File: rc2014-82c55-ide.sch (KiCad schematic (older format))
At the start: 22 parts, among them J1 CONN_01X02, J2 IDE connector, J3 IDE connector, J5 CONN_01X03, P1 RC2014 BUS, SW1 SW_DIP_x06, U1 82C55A_PLCC, U2 74HCT688, U3 74HCT04

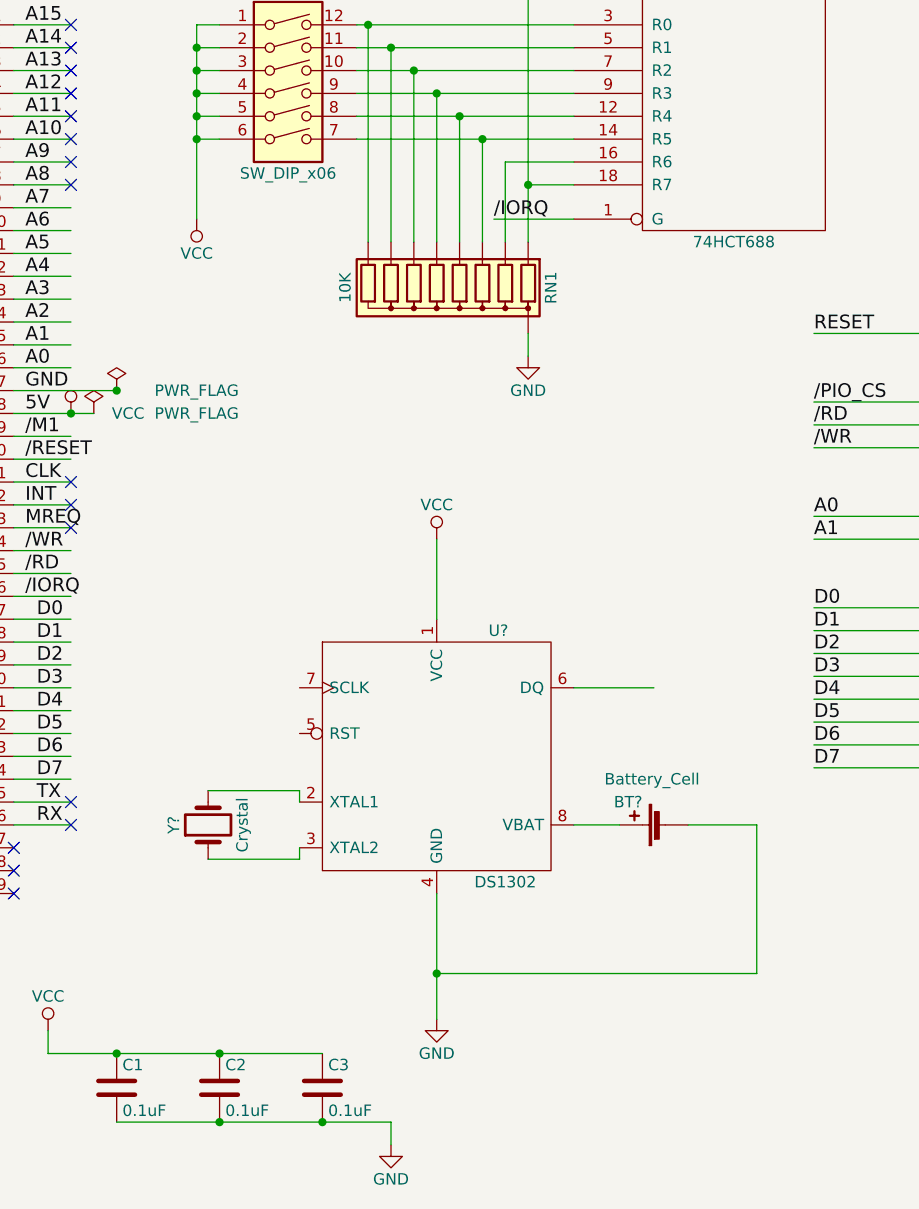
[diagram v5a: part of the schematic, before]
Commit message: remove clock
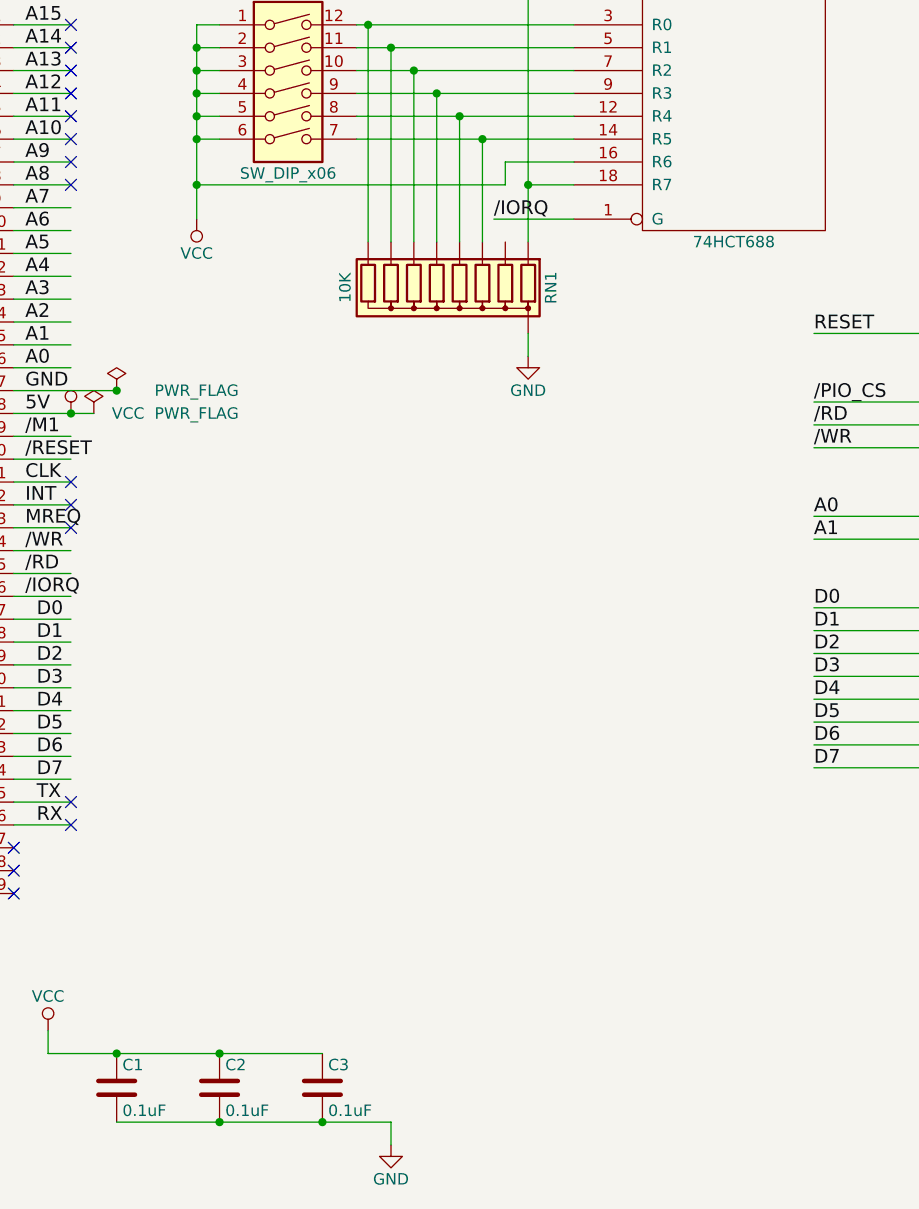
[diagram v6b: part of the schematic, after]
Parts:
- removed BT?: Battery_Cell, symbol Battery_Cell
- removed U?: DS1302, symbol DS1302
- removed Y?: Crystal, symbol Crystal
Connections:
- wire segments 243 -> 233
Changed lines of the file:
@@
 	3350 1650 3350 2750
-Wire Wire Line
-	3250 2750 3250 2400
 Wire Wire Line
 	3150 2750 3150 2300
@@
 Text Label 8650 4900 0    60   ~ 0
 DIOR
-$Comp
-L DS1302 U?
-U 1 1 59C5373F
-P 2950 5000
-F 0 "U?" H 3220 5550 50  0000 C CNN
-F 1 "DS1302" H 3250 4450 50  0000 C CNN
-F 2 "" H 2950 5000 50  0000 C CNN
-F 3 "" H 2950 5000 50  0000 C CNN
-	1    2950 5000
-	1    0    0    -1
-$EndComp
-$Comp
-L Crystal Y?
-U 1 1 59C537A8
-P 1950 5300
-F 0 "Y?" H 1950 5450 50  0000 C CNN
-F 1 "Crystal" H 1950 5150 50  0000 C CNN
-F 2 "" H 1950 5300 50  0000 C CNN
-F 3 "" H 1950 5300 50  0000 C CNN
-	1    1950 5300
-	0    -1   -1   0
-$EndComp
-$Comp
-L Battery_Cell BT?
-U 1 1 59C53806
-P 3950 5300
-F 0 "BT?" V 4050 5400 50  0000 L CNN
-F 1 "Battery_Cell" V 4150 5150 50  0000 L CNN
-F 2 "" V 3950 5360 50  0000 C CNN
-F 3 "" V 3950 5360 50  0000 C CNN
-	1    3950 5300
-	0    -1   -1   0
-$EndComp
-Wire Wire Line
-	2950 4050 2950 4400
-Wire Wire Line
-	2950 5600 2950 6150
-Wire Wire Line
-	3550 4700 3900 4700
-Wire Wire Line
-	3750 5300 3550 5300
-Wire Wire Line
-	4050 5300 4350 5300
-Wire Wire Line
-	4350 5300 4350 5950
-Wire Wire Line
-	4350 5950 2950 5950
-Connection ~ 2950 5950
-$Comp
-L GND #PWR?
-U 1 1 59C54569
-P 2950 6150
-F 0 "#PWR?" H 2950 5900 50  0001 C CNN
-F 1 "GND" H 2950 6000 50  0000 C CNN
-F 2 "" H 2950 6150 50  0000 C CNN
-F 3 "" H 2950 6150 50  0000 C CNN
-	1    2950 6150
-	1    0    0    -1
-$EndComp
-$Comp
-L VCC #PWR?
-U 1 1 59C545CE
-P 2950 4050
-F 0 "#PWR?" H 2950 3900 50  0001 C CNN
-F 1 "VCC" H 2950 4200 50  0000 C CNN
-F 2 "" H 2950 4050 50  0000 C CNN
-F 3 "" H 2950 4050 50  0000 C CNN
-	1    2950 4050
-	1    0    0    -1
-$EndComp
-Wire Wire Line
-	1950 5450 2350 5450
-Wire Wire Line
-	2350 5450 2350 5400
-Wire Wire Line
-	2350 5200 2350 5150
-Wire Wire Line
-	2350 5150 1950 5150
+Wire Wire Line
+	3250 2400 3250 2500
+Wire Wire Line
+	3250 2500 1900 2500
+Connection ~ 1900 2500
 $EndSCHEMATC

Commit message: WIP
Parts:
- JP1, JP2, JP3, JP4: footprint (none) -> Pin_Headers:Pin_Header_Straight_1x03_Pitch2.54mm
- RN1: footprint Resistors_THT:R_Array_SIP9 -> Resistors_THT:R_Array_SIP8; symbol R_Network08 -> R_Network07
- SW1: symbol SW_DIP_x06 -> SW_DIP_x06-RESCUE-rc2014-82c55-ide
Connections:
- wire segments 233 -> 234

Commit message: R1 as submitted to allpcb
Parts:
- added R2, R3, R4: 10K, Resistors_THT:R_Axial_DIN0207_L6.3mm_D2.5mm_P7.62mm_Horizontal, symbol R
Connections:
- net labels added: CSEL, DMACK, DMARQ
- wire segments 234 -> 242
- no-connect marks 32 -> 26
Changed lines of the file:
@@
 Text Label 8950 3200 0    60   ~ 0
 DA2
-NoConn ~ 7650 2500
 NoConn ~ 7650 2800
-NoConn ~ 7650 2900
-NoConn ~ 9150 2800
 NoConn ~ 9150 3000
 NoConn ~ 9150 3100
@@
 Text Label 10650 3200 0    60   ~ 0
 DA2
-NoConn ~ 9350 2500
 NoConn ~ 9350 2800
-NoConn ~ 9350 2900
-NoConn ~ 10850 2800
 NoConn ~ 10850 3000
 NoConn ~ 10850 3100
@@
 Text Label 7950 5200 0    60   ~ 0
 PC6
+Text Label 7650 2500 0    60   ~ 0
+DMARQ
+Text Label 9350 2500 0    60   ~ 0
+DMARQ
+Text Label 7650 2900 0    60   ~ 0
+DMACK
+Text Label 9350 2900 0    60   ~ 0
+DMACK
+Text Label 8750 2800 0    60   ~ 0
+CSEL
+Text Label 10450 2800 0    60   ~ 0
+CSEL
+Text Label 8700 3650 0    60   ~ 0
+CSEL
+Wire Wire Line
+	9100 3650 8600 3650
+Wire Wire Line
+	8600 3650 8600 3800
+Connection ~ 8600 3800
+Wire Wire Line
+	7500 950  7850 950
+$Comp
+L R R3
+U 1 1 59C99AC5
+P 8000 950
+F 0 "R3" V 8080 950 50  0000 C CNN
+F 1 "10K" V 8000 950 50  0000 C CNN
+F 2 "Resistors_THT:R_Axial_DIN0207_L6.3mm_D2.5mm_P7.62mm_Horizontal" V 7930 950 50  0001 C CNN
+F 3 "" H 8000 950 50  0001 C CNN
+	1    8000 950
+	0    1    1    0
+$EndComp
+Text Label 7550 950  0    60   ~ 0
+DMARQ
+Wire Wire Line
+	8150 950  8550 950
+$Comp
+L GND #PWR014
+U 1 1 59C99E1E
+P 8550 950
+F 0 "#PWR014" H 8550 700 50  0001 C CNN
+F 1 "GND" H 8550 800 50  0000 C CNN
+F 2 "" H 8550 950 50  0001 C CNN
+F 3 "" H 8550 950 50  0001 C CNN
+	1    8550 950
+	1    0    0    -1
+$EndComp
+Wire Wire Line
+	9000 900  9350 900
+$Comp
+L R R4
+U 1 1 59C99F79
+P 9500 900
+F 0 "R4" V 9580 900 50  0000 C CNN
+F 1 "10K" V 9500 900 50  0000 C CNN
+F 2 "Resistors_THT:R_Axial_DIN0207_L6.3mm_D2.5mm_P7.62mm_Horizontal" V 9430 900 50  0001 C CNN
+F 3 "" H 9500 900 50  0001 C CNN
+	1    9500 900
+	0    1    1    0
+$EndComp
+Text Label 9050 900  0    60   ~ 0
+DMACK
+Wire Wire Line
+	9650 900  10050 900
+$Comp
+L VCC #PWR015
+U 1 1 59C99FF3
+P 10050 900
+F 0 "#PWR015" H 10050 750 50  0001 C CNN
+F 1 "VCC" H 10050 1050 50  0000 C CNN
+F 2 "" H 10050 900 50  0001 C CNN
+F 3 "" H 10050 900 50  0001 C CNN
+	1    10050 900
+	1    0    0    -1
+$EndComp
+Wire Wire Line
+	5250 1650 5600 1650
+$Comp
+L R R2
+U 1 1 59C9A0F0
+P 5750 1650
+F 0 "R2" V 5830 1650 50  0000 C CNN
+F 1 "10K" V 5750 1650 50  0000 C CNN
+F 2 "Resistors_THT:R_Axial_DIN0207_L6.3mm_D2.5mm_P7.62mm_Horizontal" V 5680 1650 50  0001 C CNN
+F 3 "" H 5750 1650 50  0001 C CNN
+	1    5750 1650
+	0    1    1    0
+$EndComp
+Text Label 5300 1650 0    60   ~ 0
+PA7
+Wire Wire Line
+	5900 1650 6300 1650
+$Comp
+L GND #PWR016
+U 1 1 59C9A0F8
+P 6300 1650
+F 0 "#PWR016" H 6300 1400 50  0001 C CNN
+F 1 "GND" H 6300 1500 50  0000 C CNN
+F 2 "" H 6300 1650 50  0001 C CNN
+F 3 "" H 6300 1650 50  0001 C CNN
+	1    6300 1650
+	1    0    0    -1
+$EndComp
 $EndSCHEMATC
